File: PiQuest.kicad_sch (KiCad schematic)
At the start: 40 parts, among them J1 AudioJack2_Ground_Switch, J2 USB_C_Receptacle_PowerOnly_6P, Q1 FS8205A_C2830320, SW1 SW_Omron_B3FS, SW10 SW_Omron_B3FS, SW11 SW_Omron_B3FS, SW12 SW_Omron_B3FS, SW14 SW_SPST, SW2 SW_Omron_B3FS, SW3 SW_Omron_B3FS, SW4 SW_Omron_B3FS, SW5 SW_Omron_B3FS, SW6 SW_Omron_B3FS, SW7 SW_Omron_B3FS, SW8 SW_Omron_B3FS, SW9 SW_Omron_B3FS, U1 TP4056-42-ESOP8, U2 MAX98357A, U3 DW01A, U4 HS24CG003-ARX, U5 MT3608

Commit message: fixed lcd footprint
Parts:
- Q1: footprint easyeda2kicad:SOT-23-6_L2.9-W1.6-P0.95-LS2.8-BR -> (none)
- U4: footprint easyeda2kicad:LCD-SMD_HS24CG003-ARX -> easyeda2kicad:lcd
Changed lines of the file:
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@@
 			)
 		)
-		(property "Footprint" "easyeda2kicad:SOT-23-6_L2.9-W1.6-P0.95-LS2.8-BR"
+		(property "Footprint" ""
 			(at 224.79 77.47 0)
 			(effects
@@
 			)
 		)
-		(property "Footprint" "easyeda2kicad:LCD-SMD_HS24CG003-ARX"
+		(property "Footprint" "easyeda2kicad:lcd"
 			(at 140.97 154.94 0)
 			(effects

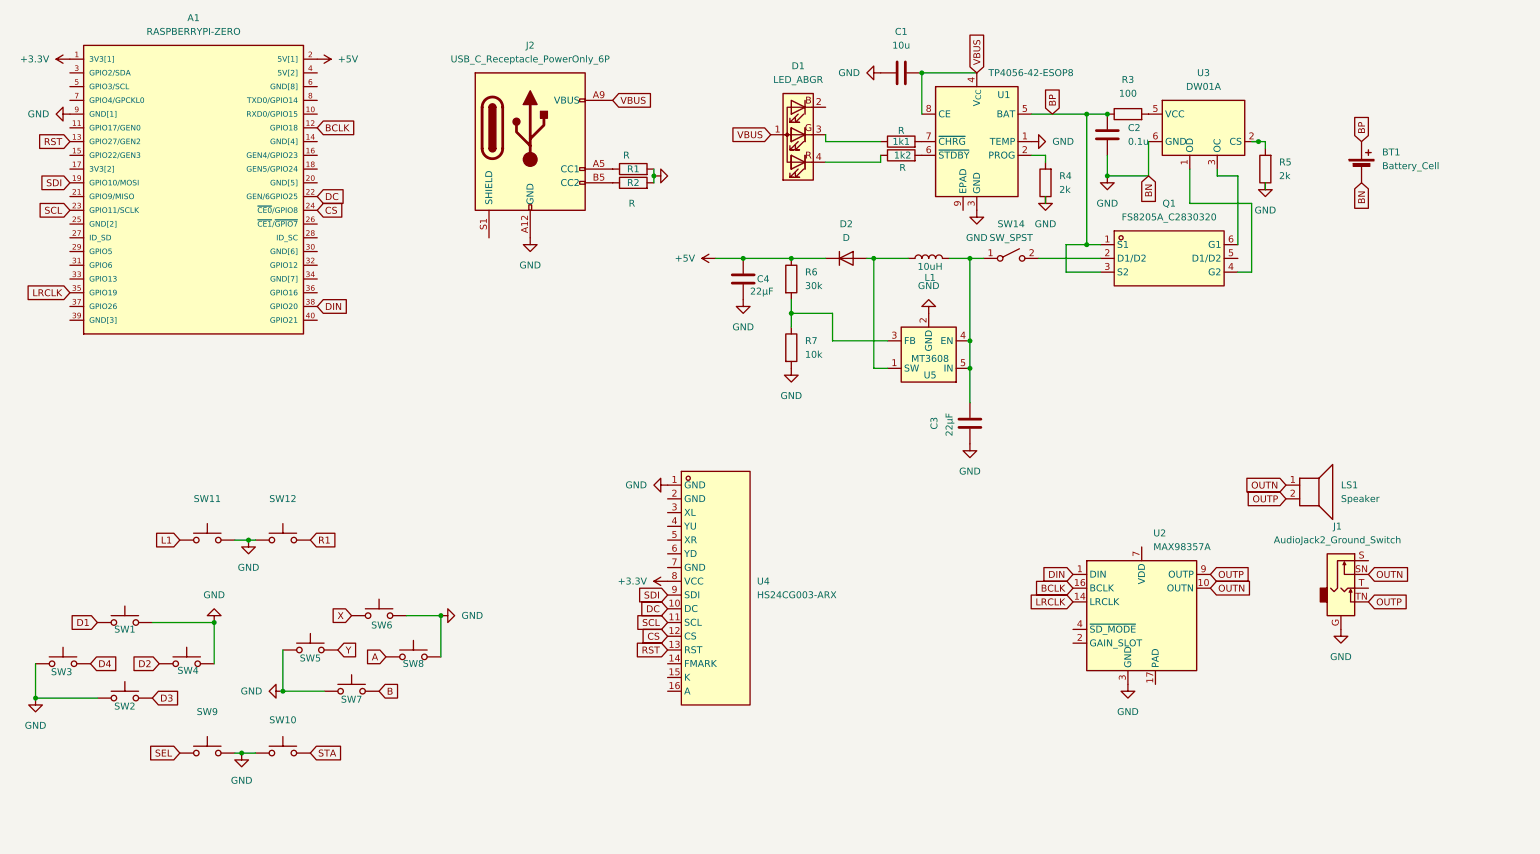
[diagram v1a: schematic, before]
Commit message: added usb c and fixed alignment issues
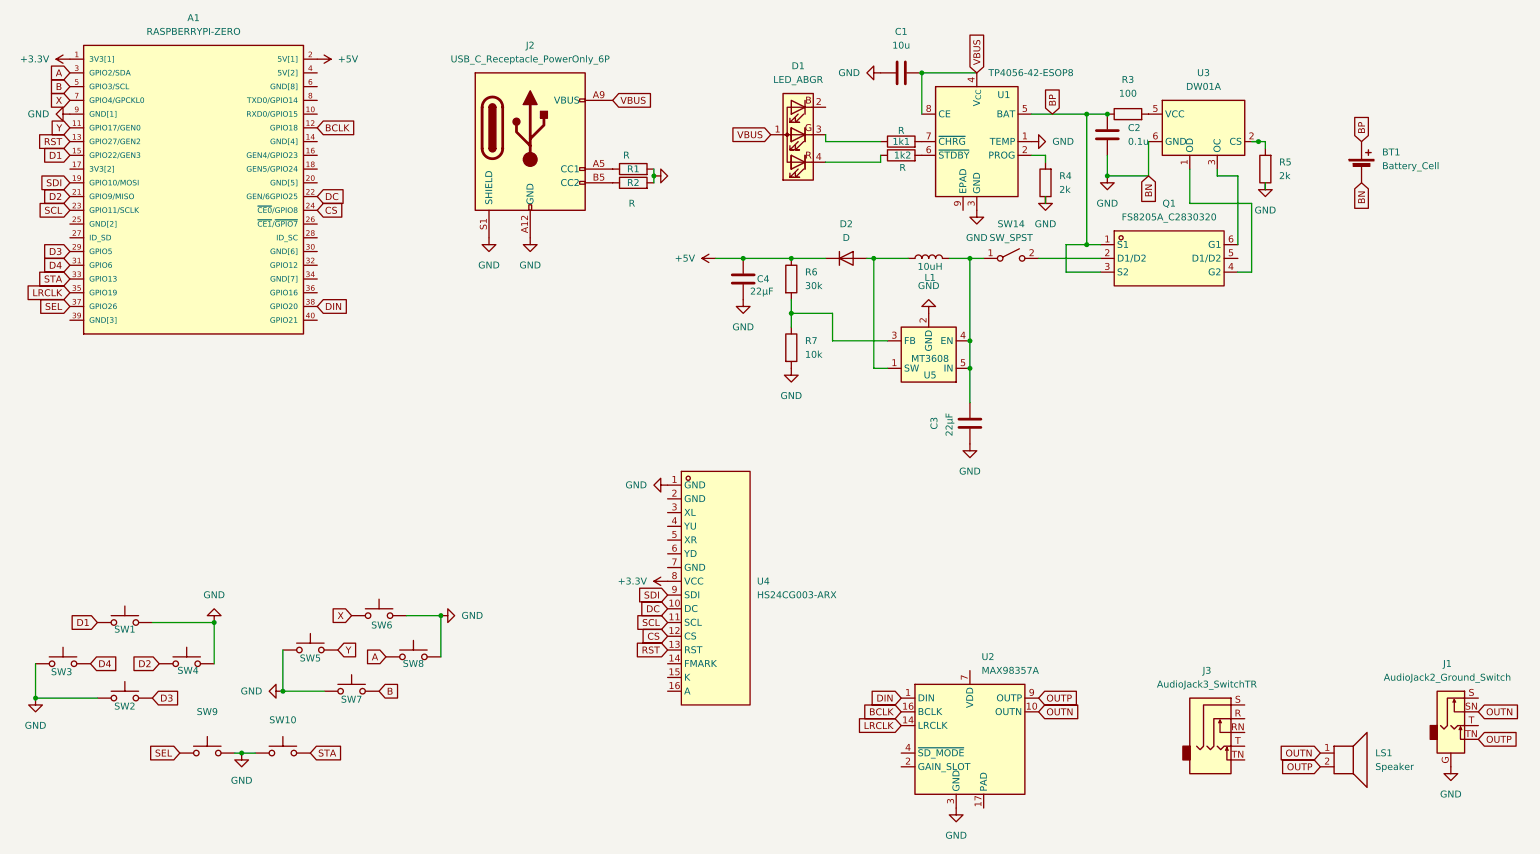
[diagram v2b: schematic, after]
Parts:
- removed SW11, SW12: SW_Omron_B3FS, symbol Switch:SW_Omron_B3FS
- added J3: AudioJack3_SwitchTR, symbol Connector_Audio:AudioJack3_SwitchTR
- 1k1, 1k2, R1, R2, R3, R4, R5, R6, R7: footprint (none) -> Resistor_SMD:R_1206_3216Metric_Pad1.30x1.75mm_HandSolder
- BT1: footprint (none) -> ScottoKeebs_Scotto:Battery
- J1: footprint (none) -> Connector_Audio:Jack_3.5mm_CUI_SJ1-3515N_Horizontal
- J2: footprint (none) -> Connector_USB:USB_C_Receptacle_HRO_TYPE-C-31-M-17
- Q1: footprint (none) -> easyeda2kicad:SOT-23-6_L2.9-W1.6-P0.95-LS2.8-BR
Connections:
- net A: now also A1.3 (GPIO2/SDA)
- net B: now also A1.5 (GPIO3/SCL)
- net D1: now also A1.15 (GPIO22/GEN3)
- net D2: now also A1.21 (GPIO9/MISO)
- net D3: now also A1.29 (GPIO5)
- net D4: now also A1.31 (GPIO6)
- net GND: now also J2.S1 (SHIELD)
- net SEL: now also A1.37 (GPIO26)
- net STA: now also A1.33 (GPIO13)
- net X: now also A1.7 (GPIO4/GPCKL0)
- net Y: now also A1.11 (GPIO17/GEN0)
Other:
- moved on the sheet: J1, LS1, U2

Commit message: better schematics
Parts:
- removed J1: AudioJack2_Ground_Switch, Connector_Audio:Jack_3.5mm_CUI_SJ1-3515N_Horizontal, symbol Connector_Audio:AudioJack2_Ground_Switch
- removed J3: AudioJack3_SwitchTR, symbol Connector_Audio:AudioJack3_SwitchTR
- removed U2: MAX98357A, Package_DFN_QFN:TQFN-16-1EP_3x3mm_P0.5mm_EP1.23x1.23mm, symbol Audio:MAX98357A
- added C10, C11, C12: 1 µF, Capacitor_SMD:C_0603_1608Metric, symbol Device:C_Small_US
- added C5, C8, C9: 0.1µF, Capacitor_SMD:C_0603_1608Metric, symbol Device:C_Small_US
- added J1: AudioJack2_Dual_Ground_Switch, symbol Connector_Audio:AudioJack2_Dual_Ground_Switch
- added R10: 22Ω, symbol Device:R
- added R8, R9: 1k, symbol Device:R
- added U2: PCM5102A, Package_SO:TSSOP-20_4.4x6.5mm_P0.65mm, symbol Audio:PCM5102A
- added U8: PAM8302AAD, symbol Amplifier_Audio:PAM8302AAD
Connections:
- net +3.3V: now also R10.1
- net DIN: now also A1.40 (GPIO21), U2.14 (DIN); no longer A1.38 (GPIO20)
- net GND: now also U4.15 (K), U4.7 (GND), C10.2, C11.2, C12.2, C5.1, C8.1, C9.1, J1.G, U2.16 (FMT), U2.17 (XSMT), U2.19 (DGND), U2.3 (CPGND), U2.9 (AGND), U8.4 (IN-), U8.7 (GND)
- net OUTN: now also U8.5 (OUT+)
- net OUTP: now also U8.8 (OUT-)
- net at U4.16 (A): now also R10.2
- net BCLK renamed BCK
- net BCK: now also U2.13 (BCK)
- net LRCLK renamed LRCK
- net LRCK: now also U2.15 (LRCK)
- new net: R8.1, R9.1, U8.3 (IN+)
- new net: C10.1, U2.2 (CAPP)
- new net: C12.1, U2.5 (VNEG)
- new net: C11.1, U2.4 (CAPM)
- new net +3V3: C5.2, C8.2, C9.2, U2.1 (CPVDD), U2.20 (DVDD), U2.8 (AVDD)
- new net OUTL: J1.S1, U2.6 (OUTL)
- new net OUTR: J1.T1, U2.7 (OUTR)
- new net SPKL: J1.SN1, R9.2
- new net SPKR: J1.TN1, R8.2
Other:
- note added: "Audio"
- note added: "Game pad"
- note added: "power"
- moved on the sheet: 1k1, 1k2, A1, BT1, C1, C2, C3, C4, D1, D2, J2, L1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
